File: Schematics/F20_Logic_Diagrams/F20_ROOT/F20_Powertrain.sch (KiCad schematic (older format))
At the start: 1 part

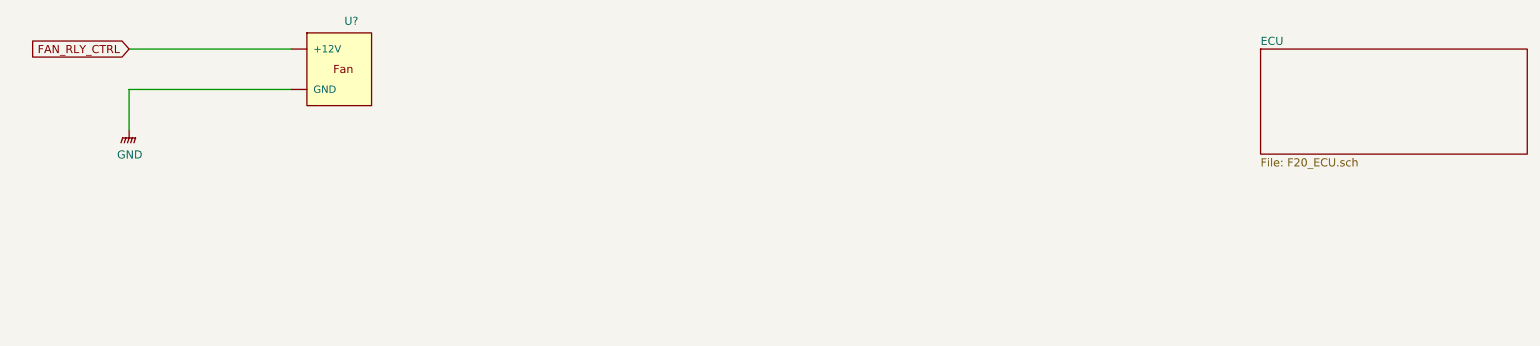
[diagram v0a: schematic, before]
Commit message: Updated per AD commit. O2 sensor schematic, transponder schematic.
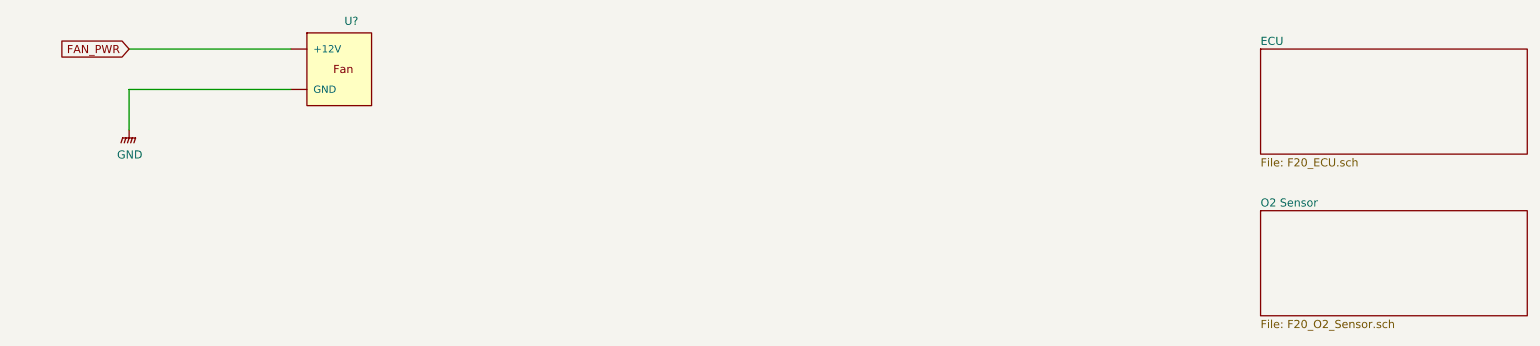
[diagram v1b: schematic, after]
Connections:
- net FAN_RLY_CTRL is gone; now on net GNDPWR: U?.~ (GND)
- new net FAN_PWR: U?.~ (GND)
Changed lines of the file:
@@
 EESchema Schematic File Version 4
-LIBS:F20_ROOT-cache
 EELAYER 30 0
 EELAYER END
 $Descr A 11000 8500
 encoding utf-8
-Sheet 2 7
+Sheet 2 9
 Title "Engine"
 Date "2020-02-03"
@@
 	1500 1250 2500 1250
 Text GLabel 1500 1000 0    50   Input ~ 0
-FAN_RLY_CTRL
+FAN_PWR
 Wire Wire Line
 	1500 1000 2500 1000
+$Sheet
+S 8500 2000 1650 650
+U 5E38FCEE
+F0 "O2 Sensor" 50
+F1 "F20_O2_Sensor.sch" 50
+$EndSheet
 $EndSCHEMATC

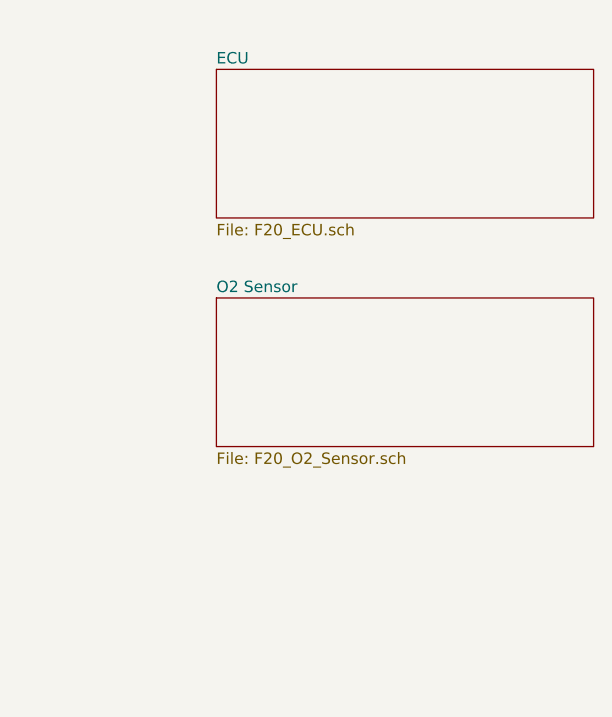
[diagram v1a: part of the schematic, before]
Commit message: Weekly update. Added Tire temp sensors drawing.
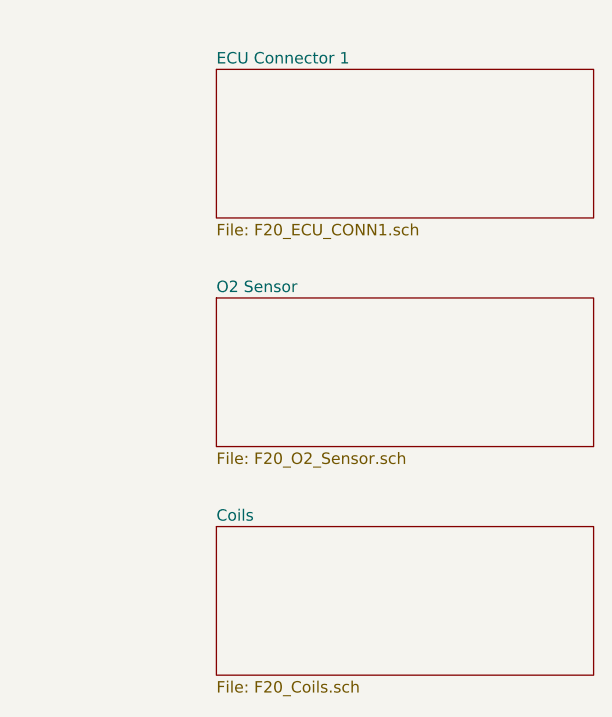
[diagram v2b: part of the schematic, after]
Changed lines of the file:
@@
 EESchema Schematic File Version 4
+LIBS:F20_ROOT-cache
 EELAYER 30 0
 EELAYER END
 $Descr A 11000 8500
 encoding utf-8
-Sheet 2 9
+Sheet 2 11
 Title "Engine"
 Date "2020-02-03"
@@
 S 8500 1000 1650 650
 U 5E3C547B
-F0 "ECU" 50
-F1 "F20_ECU.sch" 50
+F0 "ECU Connector 1" 50
+F1 "F20_ECU_CONN1.sch" 50
 $EndSheet
 $Comp
@@
 $EndComp
 $Comp
-L FSAE_Library:GND #PWR?
+L FSAE_Library:GND #PWR0101
 U 1 1 5E3D3AE8
 P 1500 1500
-F 0 "#PWR?" H 1500 1300 50  0001 C CNN
+F 0 "#PWR0101" H 1500 1300 50  0001 C CNN
 F 1 "GND" H 1504 1346 50  0000 C CNN
 F 2 "" H 1500 1450 50  0001 C CNN
@@
 F1 "F20_O2_Sensor.sch" 50
 $EndSheet
+$Sheet
+S 8500 3000 1650 650
+U 5E3A281D
+F0 "Coils" 50
+F1 "F20_Coils.sch" 50
+$EndSheet
 $EndSCHEMATC

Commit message: 02/18/20 update
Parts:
- gave numbers to parts that had none: 1
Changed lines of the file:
@@
 $Descr A 11000 8500
 encoding utf-8
-Sheet 2 11
+Sheet 2 13
 Title "Engine"
 Date "2020-02-03"
@@
 $EndSheet
 $Comp
-L FSAE_Library:Fan U?
+L FSAE_Library:Fan U1
 U 1 1 5E3D2712
 P 2500 1000
-F 0 "U?" H 2875 1173 50  0000 C CNN
+F 0 "U1" H 2875 1173 50  0000 C CNN
 F 1 "Fan" H 2750 1150 50  0001 C CNN
 F 2 "" H 3000 1500 50  0001 C CNN
@@
 $EndComp
 $Comp
-L FSAE_Library:GND #PWR0101
+L FSAE_Library:GND #PWR01
 U 1 1 5E3D3AE8
 P 1500 1500
-F 0 "#PWR0101" H 1500 1300 50  0001 C CNN
+F 0 "#PWR01" H 1500 1300 50  0001 C CNN
 F 1 "GND" H 1504 1346 50  0000 C CNN
 F 2 "" H 1500 1450 50  0001 C CNN
@@
 	1500 1000 2500 1000
 $Sheet
-S 8500 2000 1650 650
+S 8500 3000 1650 650
 U 5E38FCEE
 F0 "O2 Sensor" 50
@@
 $EndSheet
 $Sheet
-S 8500 3000 1650 650
+S 8500 4000 1650 650
 U 5E3A281D
 F0 "Coils" 50
 F1 "F20_Coils.sch" 50
 $EndSheet
+$Sheet
+S 8500 2000 1650 650
+U 5E5C9CA8
+F0 "ECU Connector 2" 50
+F1 "F20_ECU_CONN2.sch" 50
+$EndSheet
 $EndSCHEMATC

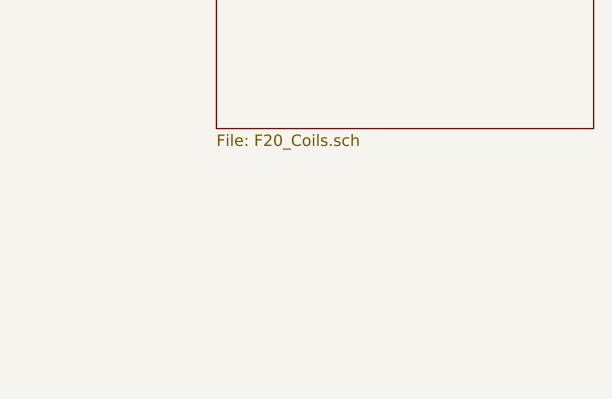
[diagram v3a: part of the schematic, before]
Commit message: Added injectors drawing
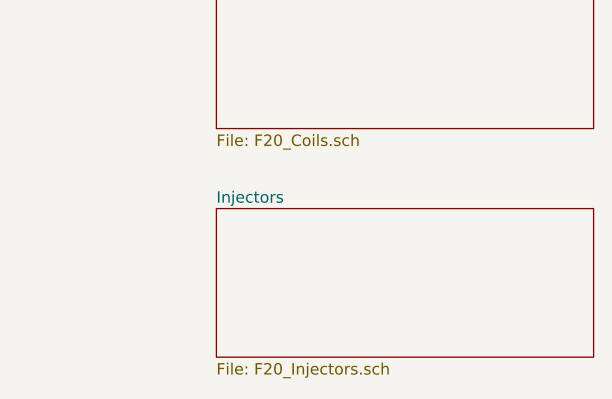
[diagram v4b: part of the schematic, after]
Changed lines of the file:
@@
 $Descr A 11000 8500
 encoding utf-8
-Sheet 2 13
+Sheet 2 14
 Title "Engine"
 Date "2020-02-03"
@@
 F1 "F20_ECU_CONN2.sch" 50
 $EndSheet
+$Sheet
+S 8500 5000 1650 650
+U 5E55FFBC
+F0 "Injectors" 50
+F1 "F20_Injectors.sch" 50
+$EndSheet
 $EndSCHEMATC
